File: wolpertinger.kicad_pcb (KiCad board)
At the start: 2 copper layers, 100.6 x 80 mm, 58 parts, among them K1 FRT5, K2 FRT5, Q1 BC549, Q2 2N5088, U1 4093, U2 TL074, U3 TL074, U4 VTL5C, U5 VTL5C, U6 VTL5C, U7 VTL5C, U8 TL072, U9 L78L05_TO92

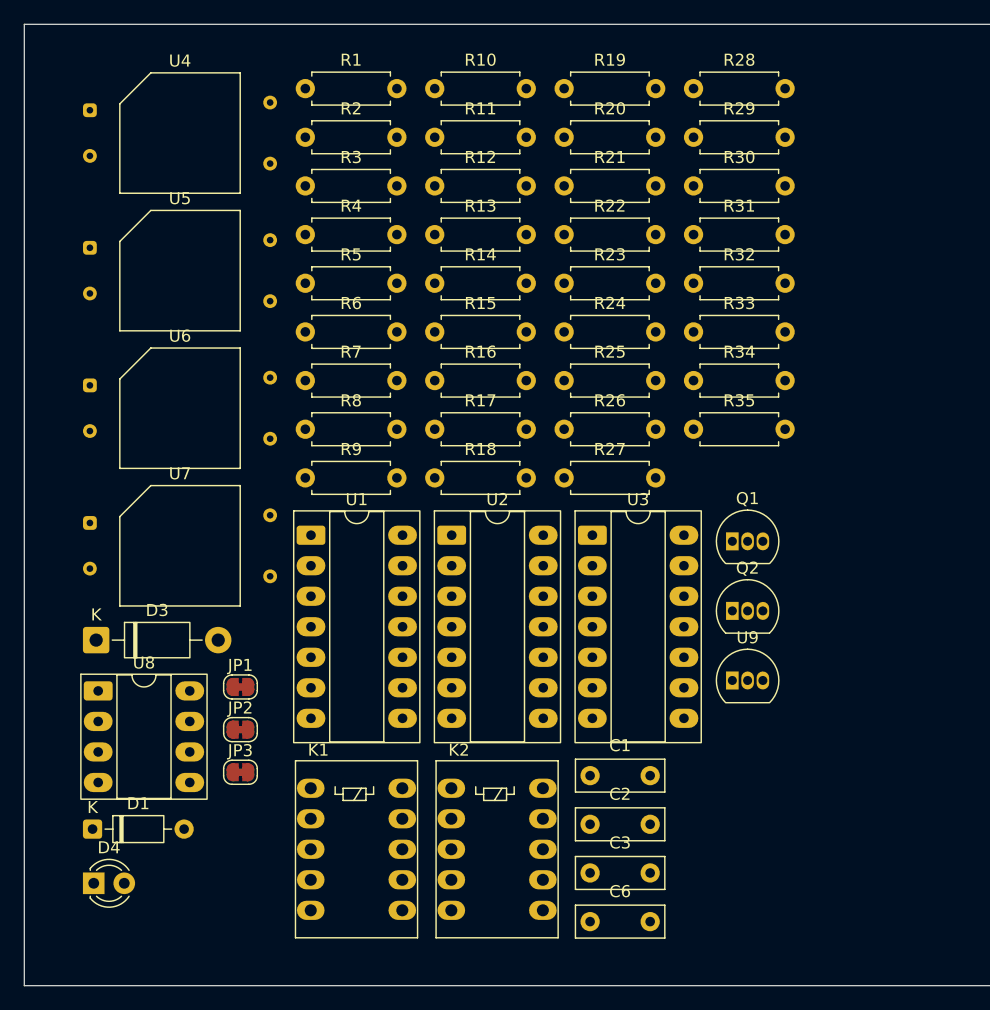
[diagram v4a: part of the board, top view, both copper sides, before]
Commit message: cleanup power supply, add lfo voltage offset
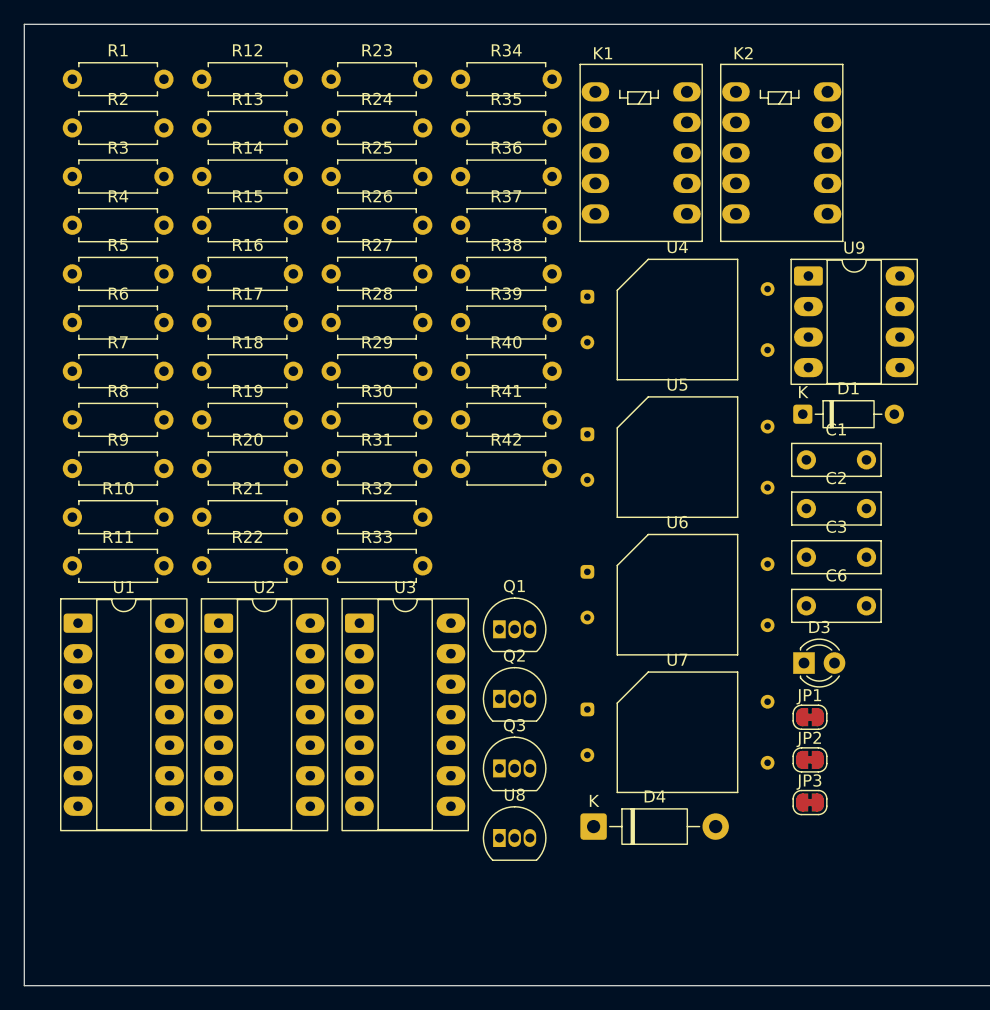
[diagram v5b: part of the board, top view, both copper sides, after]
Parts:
- added Q3: BC547, Package_TO_SOT_THT:TO-92_Inline, F.Cu at (116.2, 111.0)
- added R36: 10k, Resistor_THT:R_Axial_DIN0207_L6.3mm_D2.5mm_P7.62mm_Horizontal, F.Cu at (113.0, 61.7)
- added R37: 10k, Resistor_THT:R_Axial_DIN0207_L6.3mm_D2.5mm_P7.62mm_Horizontal, F.Cu at (113.0, 65.7)
- added R38: 10k, Resistor_THT:R_Axial_DIN0207_L6.3mm_D2.5mm_P7.62mm_Horizontal, F.Cu at (113.0, 69.8)
- added R39: 100k, Resistor_THT:R_Axial_DIN0207_L6.3mm_D2.5mm_P7.62mm_Horizontal, F.Cu at (113.0, 73.8)
- added R40: 100k, Resistor_THT:R_Axial_DIN0207_L6.3mm_D2.5mm_P7.62mm_Horizontal, F.Cu at (113.0, 77.9)
- added R41: 10k, Resistor_THT:R_Axial_DIN0207_L6.3mm_D2.5mm_P7.62mm_Horizontal, F.Cu at (113.0, 81.9)
- added R42: 10k, Resistor_THT:R_Axial_DIN0207_L6.3mm_D2.5mm_P7.62mm_Horizontal, F.Cu at (113.0, 86.0)
- D3: value 1N4001 -> TBD; footprint Diode_THT:D_DO-41_SOD81_P10.16mm_Horizontal -> LED_THT:LED_D3.0mm
- D4: value TBD -> 1N4001; footprint LED_THT:LED_D3.0mm -> Diode_THT:D_DO-41_SOD81_P10.16mm_Horizontal
- Q2: value 2N5088 -> BC547
- R23: value TBD -> 4k7
- R24: value TBD -> 33r
- R26: value 33r -> 22k
- R27: value 15k -> 3M3
- R28: value 2M2 -> 100k
- R29: value 15k -> 100k
- R30: value 33r -> 100k
- R31: value 1k -> 100k
- R32: value 100k -> 10k
- R33: value 100k -> TBD
- R34: value 100k -> 4k7
- R35: value 100k -> 33r
- U8: value TL072 -> L78L05_TO92; footprint Package_DIP:DIP-8_W7.62mm_Socket_LongPads -> Package_TO_SOT_THT:TO-92_Inline
- U9: value L78L05_TO92 -> NE5532; footprint Package_TO_SOT_THT:TO-92_Inline -> Package_DIP:DIP-8_W7.62mm_Socket_LongPads
- moved D1 68.5 mm to (141.5, 81.5)
- moved K1 62.6 mm to (124.2, 54.6)
- moved K2 62.6 mm to (135.9, 54.6)
- moved D3 58.9 mm to (141.6, 102.2)
- moved JP1 47.5 mm to (142.1, 106.7)
- moved JP2 47.5 mm to (142.1, 110.2)
- moved JP3 47.5 mm to (142.1, 113.8)
- moved R10 46.7 mm to (80.7, 90.0)
- moved R11 46.7 mm to (80.7, 94.1)
- moved U4 44.2 mm to (123.6, 71.7)
- moved U5 44.2 mm to (123.6, 83.1)
- moved U6 44.2 mm to (123.6, 94.6)
- moved U7 44.2 mm to (123.6, 106.0)
- moved D4 41.9 mm to (124.1, 115.8)
- moved R20 40.9 mm to (91.5, 86.0)
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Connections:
- D3 pad 1: Net-(D3-K) -> GND
- D3 pad 2: GND -> Net-(D3-A)
- D4 pad 1: GND -> 9V
- D4 pad 2: Net-(D4-A) -> GND
- Q2 pad 1: GND3 -> Net-(Q2-C)
- Q2 pad 3: Net-(Q2-C) -> GND3
- R23 pad 2: LFO -> GND3
- R24 pad 1: LFO -> 9V
- R24 pad 2: GND3 -> V1
- R25 pad 1: Net-(D3-K) -> 9V
- R25 pad 2: Net-(U3E-V+) -> V@
- R26 pad 1: Net-(D3-K) -> Net-(C13-Pad1)
- R26 pad 2: Net-(U2E-V+) -> GND3
- R27 pad 1: V3 -> Net-(Q2-C)
- R27 pad 2: Net-(Q2-C) -> Net-(Q2-B)
- R28 pad 1: Net-(Q2-C) -> V1
- R28 pad 2: Net-(Q2-B) -> Vref 1
- R29 pad 1: Net-(C18-Pad2) -> Vref 1
- R29 pad 2: GND3 -> GND1
- R30 pad 1: Net-(D3-K) -> V@
- R30 pad 2: Net-(U9-VI) -> Vref 2
- R31 pad 1: Net-(R31-Pad1) -> Vref 2
- R31 pad 2: GND3 -> GND2
- R32 pad 1: Net-(U3E-V+) -> V3
- R32 pad 2: Net-(U8A-+) -> Net-(Q2-C)
- R33 pad 1: Net-(U8A-+) -> Net-(Q3-E)
- R33 pad 2: GND1 -> Net-(R33-Pad2)
- R34 pad 1: V3 -> Net-(R33-Pad2)
- R34 pad 2: Vref 3 -> GND3
- R35 pad 1: Vref 3 -> 9V
- R35 pad 2: GND3 -> Net-(U8-VI)
- U2 pad 4: Net-(U2E-V+) -> V2
- U3 pad 4: Net-(U3E-V+) -> V1
- U8 pad 1: Vref 2 -> V3
- U8 pad 2: Vref 2 -> Net-(D3-A)
- U8 pad 3: Net-(U8A-+) -> Net-(U8-VI)
- U9 pad 1: V3 -> LFO
- U9 pad 2: Net-(D4-A) -> Net-(U9A--)
- U9 pad 3: Net-(U9-VI) -> Vref 3

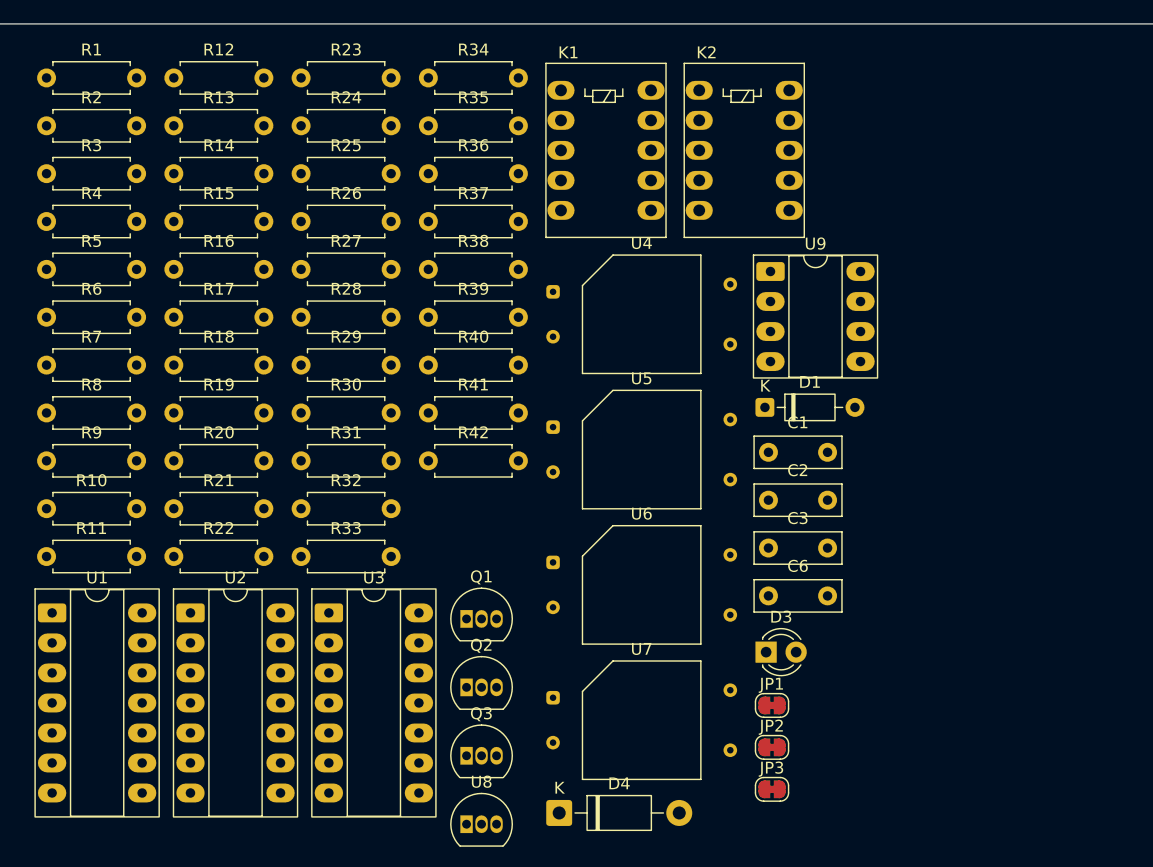
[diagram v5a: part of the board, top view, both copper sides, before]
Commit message: add custom part libary and add mode switch
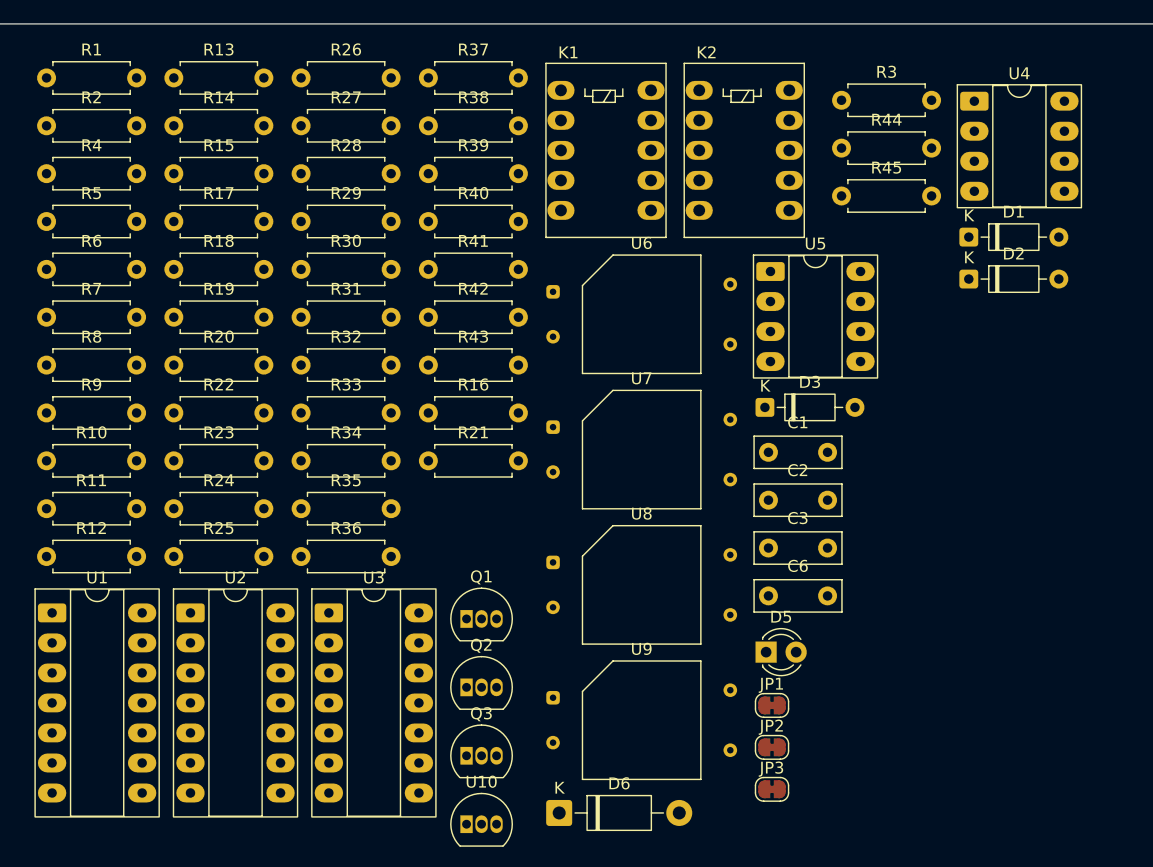
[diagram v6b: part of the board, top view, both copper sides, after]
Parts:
- added D1: BAT42, Diode_THT:D_DO-35_SOD27_P7.62mm_Horizontal, F.Cu at (158.8, 67.1)
- added D2: BAT42, Diode_THT:D_DO-35_SOD27_P7.62mm_Horizontal, F.Cu at (158.8, 70.6)
- added R3: 10k, Resistor_THT:R_Axial_DIN0207_L6.3mm_D2.5mm_P7.62mm_Horizontal, F.Cu at (148.0, 55.5)
- added R44: 100r, Resistor_THT:R_Axial_DIN0207_L6.3mm_D2.5mm_P7.62mm_Horizontal, F.Cu at (148.0, 59.5)
- added R45: 100r, Resistor_THT:R_Axial_DIN0207_L6.3mm_D2.5mm_P7.62mm_Horizontal, F.Cu at (148.0, 63.6)
- added U4: NE5532, Package_DIP:DIP-8_W7.62mm_Socket_LongPads, F.Cu at (159.2, 55.6)
- renumbered D1 to D3, D3 to D5, D4 to D6, R9 to R10, R10 to R11, R11 to R12, R12 to R13, R13 to R14, R14 to R15, R41 to R16, R15 to R17, R16 to R18, R17 to R19, R18 to R20, R42 to R21, R19 to R22, R20 to R23, R21 to R24, R22 to R25, R23 to R26, R24 to R27, R25 to R28, R26 to R29, R27 to R30, R28 to R31, R29 to R32, R30 to R33, R31 to R34, R32 to R35, R33 to R36, R34 to R37, R35 to R38, R36 to R39, R3 to R4, R37 to R40, R38 to R41, R39 to R42, R40 to R43, R4 to R5, R5 to R6, R6 to R7, R7 to R8, R8 to R9, U8 to U10, U9 to U5, U4 to U6, U5 to U7, U6 to U8, U7 to U9
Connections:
- net Net-(R42-Pad1) renamed LFO out
- R16 pad 2: unconnected-(R41-Pad2) -> LFO out inv
- R28 pad 2: V@ -> V2
- R33 pad 1: V@ -> V2
- U6 pad 1: unconnected-(U4---Pad1) -> GND3
- U6 pad 2: unconnected-(U4-+-Pad2) -> loL
- U7 pad 1: unconnected-(U5---Pad1) -> GND3
- U7 pad 2: unconnected-(U5-+-Pad2) -> hiL
- U8 pad 1: unconnected-(U6---Pad1) -> GND3
- U8 pad 2: unconnected-(U6-+-Pad2) -> loR
- U9 pad 1: unconnected-(U7---Pad1) -> GND3
- U9 pad 2: unconnected-(U7-+-Pad2) -> hiR

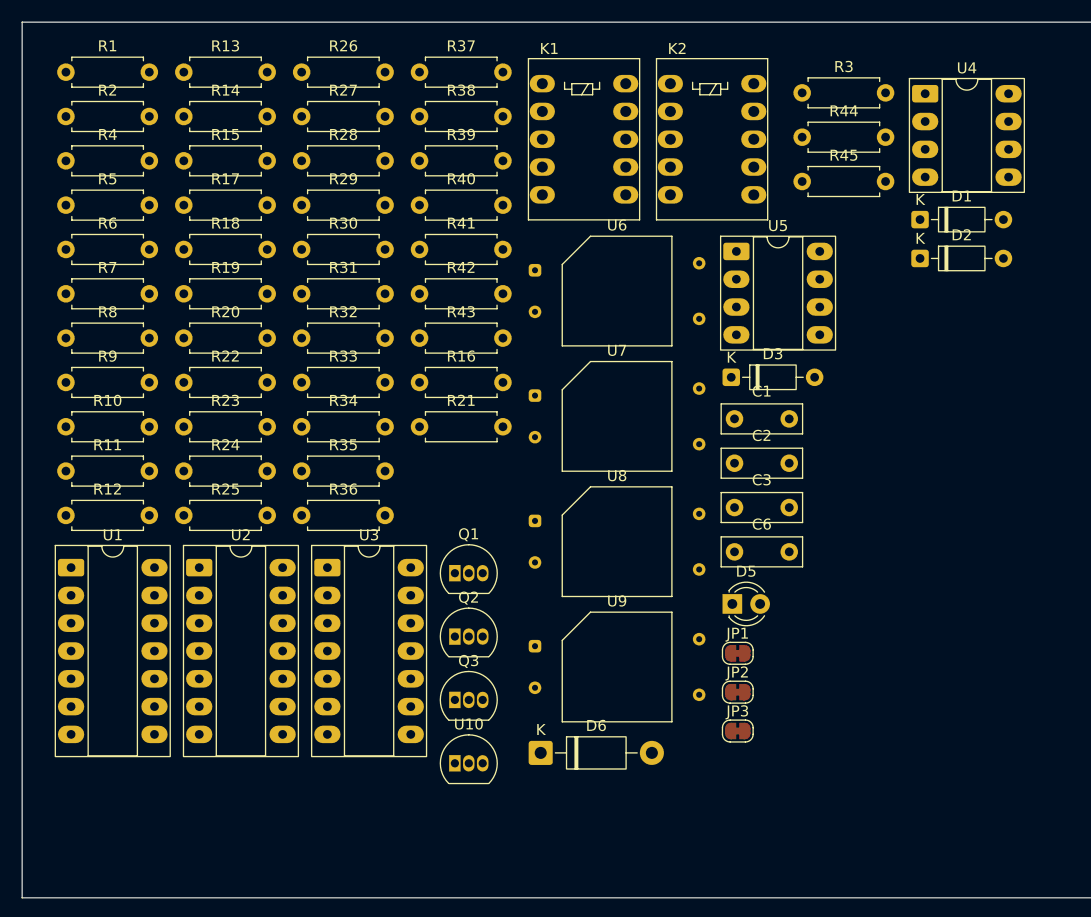
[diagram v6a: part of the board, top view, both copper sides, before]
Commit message: remove hi and low only mode in favor of simpler switches
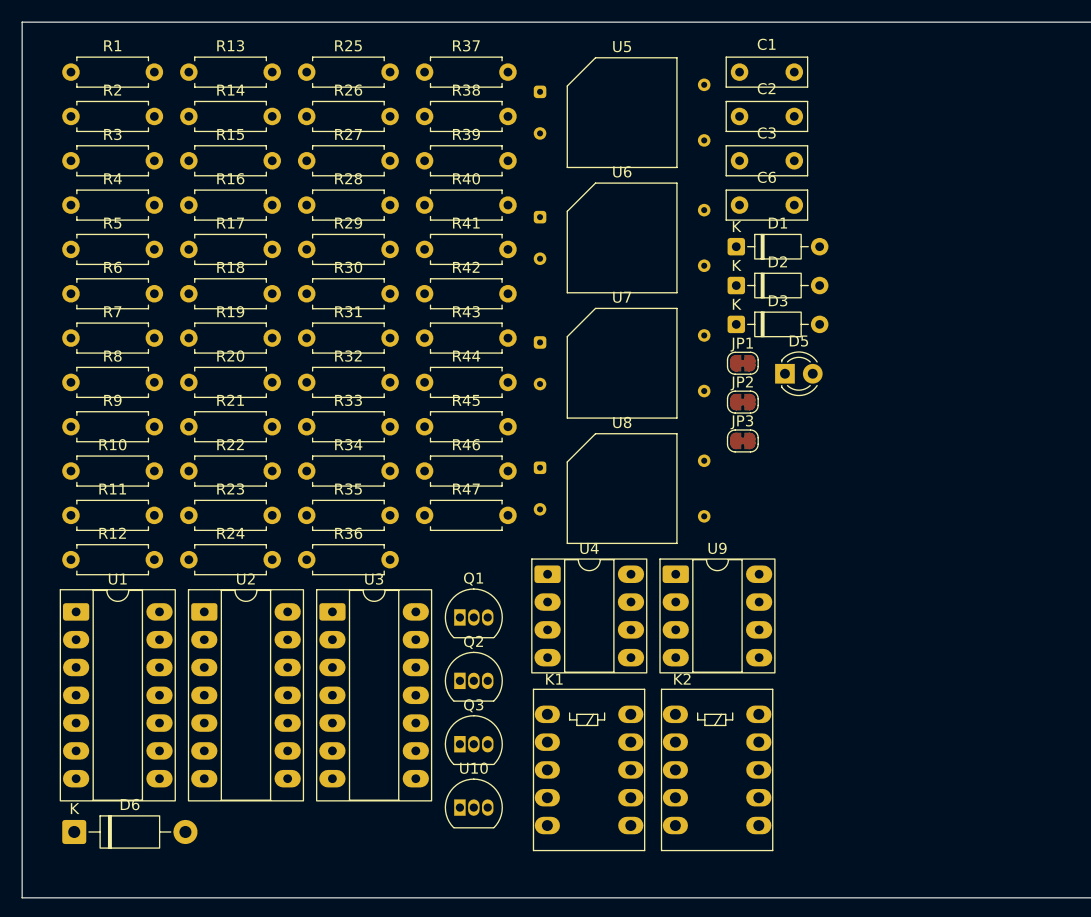
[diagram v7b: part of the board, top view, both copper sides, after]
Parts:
- added R46: 100r, Resistor_THT:R_Axial_DIN0207_L6.3mm_D2.5mm_P7.62mm_Horizontal, F.Cu at (113.5, 90.0)
- added R47: 100r, Resistor_THT:R_Axial_DIN0207_L6.3mm_D2.5mm_P7.62mm_Horizontal, F.Cu at (113.5, 94.1)
- R16: value 10k -> 51K
- R20: value 51K -> 10k
- R26: value 4k7 -> 33r
- R28: value 33r -> 4k7
- R29: value 22k -> 100r
- R3: value 10k -> 1M
- R30: value 3M3 -> 100k
- R34: value 100k -> 22k
- R35: value 10k -> 3M3
- R36: value TBD -> 100r
- R37: value 4k7 -> 10k
- R39: value 10k -> TBD
- R40: value 10k -> 4k7
- R42: value 100k -> 10k
- R44: value 100r -> 100k
- R45: value 100r -> 10k
- R5: value 1M -> 10k
- U5: value NE5532 -> VTL5C; footprint Package_DIP:DIP-8_W7.62mm_Socket_LongPads -> OptoDevice:PerkinElmer_VTL5C
- U9: value VTL5C -> NE5532; footprint OptoDevice:PerkinElmer_VTL5C -> Package_DIP:DIP-8_W7.62mm_Socket_LongPads
- moved R3 67.1 mm to (81.2, 61.7)
- moved K1 57.6 mm to (124.7, 112.3)
- moved K2 57.6 mm to (136.4, 112.3)
- moved U4 55.8 mm to (124.7, 99.5)
- moved D6 43.2 mm to (81.5, 123.0)
- moved R25 42.0 mm to (102.7, 53.6)
- moved R44 41.1 mm to (113.5, 81.9)
- moved R45 41.1 mm to (113.5, 86.0)
- moved C1 31.7 mm to (142.3, 53.6)
- moved C2 31.7 mm to (142.3, 57.6)
- moved C3 31.7 mm to (142.3, 61.7)
- moved C6 31.7 mm to (142.3, 65.7)
- moved R16 26.6 mm to (91.9, 65.7)
- moved JP2 26.5 mm to (142.6, 83.7)
- moved JP3 26.5 mm to (142.6, 87.3)
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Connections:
- R16 pad 1: Net-(U5B--) -> Net-(U2C--)
- R16 pad 2: LFO out inv -> Net-(C9-Pad2)
- R17 pad 1: Net-(U2C--) -> Net-(U3C--)
- R17 pad 2: Net-(C9-Pad2) -> Net-(C10-Pad2)
- R18 pad 1: Net-(U3C--) -> Net-(R18-Pad1)
- R18 pad 2: Net-(C10-Pad2) -> Net-(U3B--)
- R19 pad 2: Net-(U3B--) -> Net-(U2B--)
- R20 pad 1: Net-(R20-Pad1) -> Net-(U9B--)
- R20 pad 2: Net-(U2B--) -> LFO out inv
- R21 pad 2: Net-(U5B--) -> Net-(U9B--)
- R26 pad 1: Net-(R26-Pad1) -> 9V
- R26 pad 2: GND3 -> V1
- R27 pad 2: V1 -> V2
- R28 pad 1: 9V -> Net-(R28-Pad1)
- R28 pad 2: V2 -> GND3
- R29 pad 2: GND3 -> Net-(R29-Pad2)
- R3 pad 1: Net-(J3-PadT) -> Vref1
- R3 pad 2: Net-(D1-A) -> Net-(U2A-+)
- R30 pad 1: Net-(Q2-C) -> V1
- R30 pad 2: Net-(Q2-B) -> Vref 1
- R31 pad 1: V1 -> Vref 1
- R31 pad 2: Vref 1 -> GND1
- R32 pad 1: Vref 1 -> V2
- R32 pad 2: GND1 -> Vref 2
- R33 pad 1: V2 -> Vref 2
- R33 pad 2: Vref 2 -> GND2
- R34 pad 1: Vref 2 -> Net-(C19-Pad1)
- R34 pad 2: GND2 -> GND3
- R35 pad 1: V3 -> Net-(Q2-C)
- R35 pad 2: Net-(Q2-C) -> Net-(Q2-B)
- R36 pad 1: Net-(Q3-E) -> Net-(SW2B-B)
- R37 pad 1: Net-(R36-Pad2) -> V3
- R37 pad 2: GND3 -> Net-(Q2-C)
- R39 pad 1: Net-(U5A--) -> Net-(Q3-E)
- R4 pad 1: Vref1 -> Vref2
- R4 pad 2: Net-(U2A-+) -> Net-(U3A-+)
- R40 pad 1: Net-(U5A--) -> Net-(R39-Pad2)
- R40 pad 2: Net-(R36-Pad2) -> GND3
- R41 pad 1: LFO -> Net-(U9A--)
- R41 pad 2: Net-(U5A--) -> Net-(R41-Pad2)
- R42 pad 1: V3 -> Net-(U9A--)
- R42 pad 2: Vref 3 -> Net-(R39-Pad2)
- R43 pad 1: Vref 3 -> V3
- R43 pad 2: GND3 -> Vref 3
- R44 pad 1: Net-(R44-Pad1) -> Vref 3
- R44 pad 2: Net-(R44-Pad2) -> GND3
- R45 pad 1: Net-(SW2B-A) -> LFO
- R45 pad 2: Net-(R45-Pad2) -> Net-(U9A--)
- R5 pad 1: Vref2 -> Net-(J3-PadT)
- R5 pad 2: Net-(U3A-+) -> Net-(D1-A)
- U2 pad 7: Net-(R20-Pad1) -> Net-(R19-Pad1)
- U3 pad 7: Net-(R19-Pad1) -> Net-(R18-Pad1)
- U5 pad 1: LFO -> GND3
- U5 pad 2: Net-(U5A--) -> loL
- U5 pad 3: Vref 3 -> Net-(C9-Pad2)
- U5 pad 4: GND3 -> Net-(U2D--)
- U6 pad 2: loL -> hiL
- U6 pad 3: Net-(C9-Pad2) -> Net-(R19-Pad1)
- U7 pad 2: hiL -> loR
- U7 pad 3: Net-(R20-Pad1) -> Net-(C10-Pad2)
- U7 pad 4: Net-(U2D--) -> Net-(U3D--)
- U8 pad 2: loR -> hiR
- U8 pad 3: Net-(C10-Pad2) -> Net-(R18-Pad1)
- U9 pad 1: GND3 -> LFO
- U9 pad 2: hiR -> Net-(U9A--)
- U9 pad 3: Net-(R19-Pad1) -> Vref 3
- U9 pad 4: Net-(U3D--) -> GND3

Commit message: update pcb
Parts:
- added RV1: 100k B, potentiometers:16MM_PADS.1, F.Cu at (150.5, 99.3)
- added RV2: 10k B, potentiometers:16MM_PADS.1, F.Cu at (150.5, 104.3)
- added RV3: 10k B, potentiometers:16MM_PADS.1, F.Cu at (150.5, 109.2)
- added RV4: 100k C, potentiometers:16MM_PADS.1, F.Cu at (150.5, 114.1)
- added SW1: ON/OFF, switches:SPST, F.Cu at (170.4, 114.4)
- added SW2: DPDT MONO/STEREO, switches:DPDT, F.Cu at (158.0, 117.0)
- added SW3: DPDT HARMONIC/TREMOLO, switches:DPDT, F.Cu at (164.2, 117.0)
- added TR1: VOLUME Trim 50k, Potentiometer_THT:Potentiometer_Piher_PT-6-V_Vertical, F.Cu at (156.5, 102.8)
- added TR2: VOLUME Trim 50k, Potentiometer_THT:Potentiometer_Piher_PT-6-V_Vertical, F.Cu at (164.6, 102.8)
- added TR3: LO L Trim 5k, Potentiometer_THT:Potentiometer_Piher_PT-6-V_Vertical, F.Cu at (172.8, 102.8)
- added TR4: HI L Trim 5k, Potentiometer_THT:Potentiometer_Piher_PT-6-V_Vertical, F.Cu at (181.0, 102.8)
- added TR5: OFFSET Trim 25k, Potentiometer_THT:Potentiometer_Piher_PT-6-V_Vertical, F.Cu at (156.5, 111.0)
- added TR6: LO R Trim 5k, Potentiometer_THT:Potentiometer_Piher_PT-6-V_Vertical, F.Cu at (164.6, 111.0)
- added TR7: HI R Trim 5k, Potentiometer_THT:Potentiometer_Piher_PT-6-V_Vertical, F.Cu at (172.8, 111.0)
- renumbered C6 to C7
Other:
- board size 100.6 x 80 mm -> 119.6 x 80 mm
